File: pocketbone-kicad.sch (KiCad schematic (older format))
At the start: 73 parts, among them P1 USB_OTG, P2 USB_OTG, P3 CONN_01X10, SW1 SW_PUSH_SMALL_H, SW2 SW_PUSH_SMALL_H, U1 SN74LVC1G07, U2 OSD3358, U3 24LC32AT-I/OT, U4 TPS2051C, Y2 24MHz

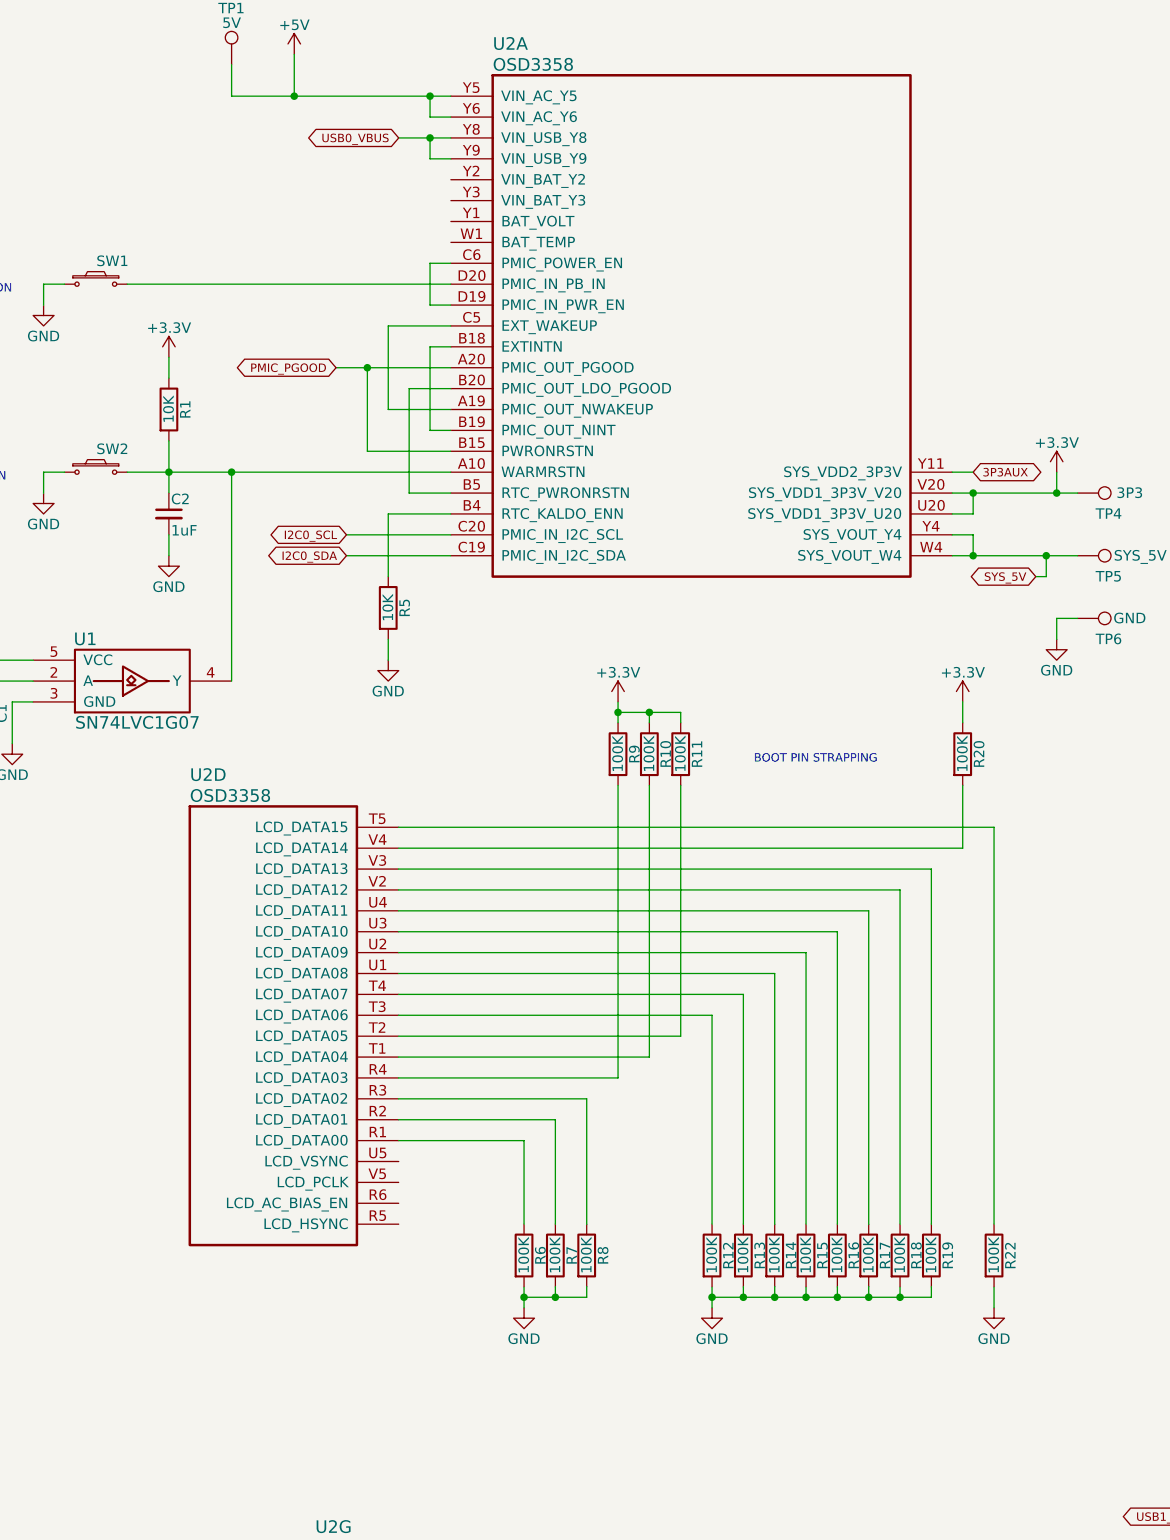
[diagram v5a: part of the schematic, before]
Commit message: Many PCB updates
Updated the placement for single sided population.
Switched boot mode selection resistors to arrays to save space.
Switched expansion header to .1 inch (lichen pub compatible).
Added battery connect similar to BBB.

Signed-off-by: Michael Welling <mwelling@ieee.org>
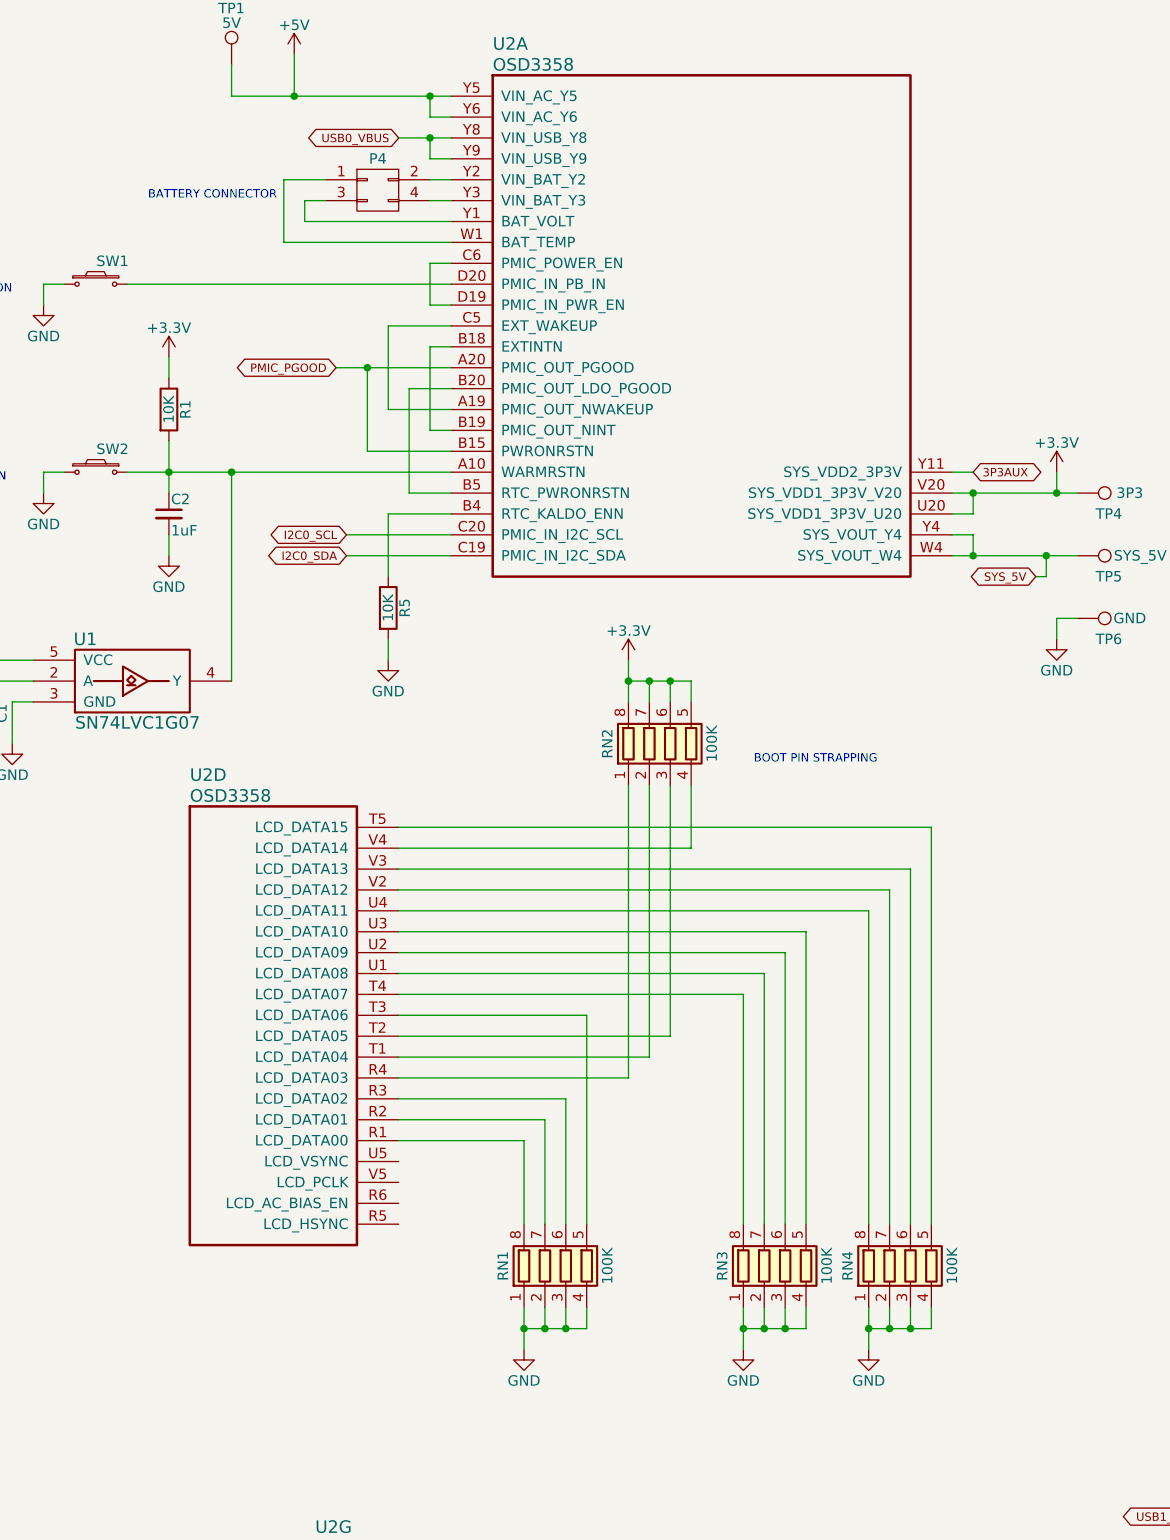
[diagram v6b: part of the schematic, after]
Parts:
- removed R10, R11, R12, R13, R14, R15, R16, R17, R18, R19, R20, R22, R6, R7, R8, R9: 100K, Resistors_SMD:R_0402, symbol R
- added P4: CONN_02X02, Socket_Strips:Socket_Strip_Straight_2x02, symbol CONN_02X02
- added RN1, RN2, RN3, RN4: 100K, Resistors_SMD:R_Array_Concave_4x0603, symbol R_Pack04
- P3: footprint Connectors_Molex:Connector_Molex_PicoBlade_53398-1071 -> Socket_Strips:Socket_Strip_Straight_1x10
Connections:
- net +3V3: now also RN2.5 (R4.2), RN2.6 (R3.2), RN2.7 (R2.2), RN2.8 (R1.2)
- net GND: now also RN1.1 (R1.1), RN1.2 (R2.1), RN1.3 (R3.1), RN1.4 (R4.1), RN3.1 (R1.1), RN3.2 (R2.1), RN3.3 (R3.1), RN3.4 (R4.1), RN4.1 (R1.1), RN4.2 (R2.1), RN4.3 (R3.1), RN4.4 (R4.1)
- net at U2.W1 (BAT_TEMP): now also P4.1 (P1)
- net at U2.Y1 (BAT_VOLT): now also P4.3 (P3)
- net at U2.Y2 (VIN_BAT_Y2): now also P4.2 (P2)
- net at U2.Y3 (VIN_BAT_Y3): now also P4.4 (P4)
- net at U2.R1 (LCD_DATA00): now also RN1.8 (R1.2)
- net at U2.R2 (LCD_DATA01): now also RN1.7 (R2.2)
- net at U2.R3 (LCD_DATA02): now also RN1.6 (R3.2)
- net at U2.R4 (LCD_DATA03): now also RN2.1 (R1.1)
- net at U2.T1 (LCD_DATA04): now also RN2.2 (R2.1)
- net at U2.T2 (LCD_DATA05): now also RN2.3 (R3.1)
- net at U2.T3 (LCD_DATA06): now also RN1.5 (R4.2)
- net at U2.T4 (LCD_DATA07): now also RN3.8 (R1.2)
- net at U2.T5 (LCD_DATA15): now also RN4.5 (R4.2)
- net at U2.U1 (LCD_DATA08): now also RN3.7 (R2.2)
- net at U2.U2 (LCD_DATA09): now also RN3.6 (R3.2)
- net at U2.U3 (LCD_DATA10): now also RN3.5 (R4.2)
- net at U2.U4 (LCD_DATA11): now also RN4.8 (R1.2)
- net at U2.V2 (LCD_DATA12): now also RN4.7 (R2.2)
- net at U2.V3 (LCD_DATA13): now also RN4.6 (R3.2)
- net at U2.V4 (LCD_DATA14): now also RN2.4 (R4.1)
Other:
- note added: "BATTERY CONNECTOR"

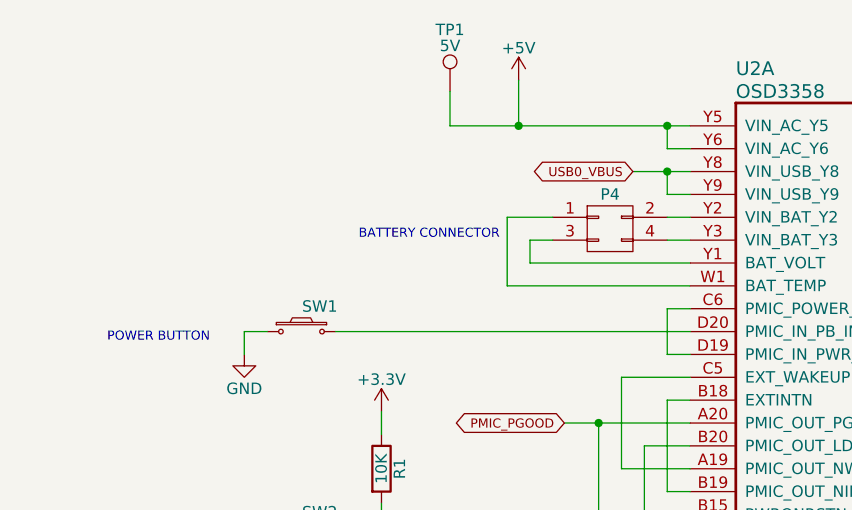
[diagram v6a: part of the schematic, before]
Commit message: Routing complete
Battery header updated in schmatic.
Plots and pictures updated.
Ready for design review.

Signed-off-by: Michael Welling <mwelling@ieee.org>
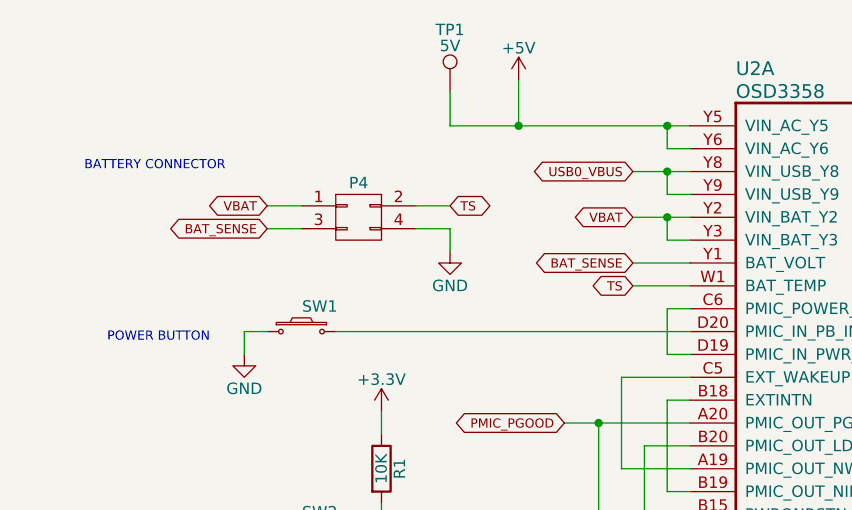
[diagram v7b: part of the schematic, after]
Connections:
- net GND: now also P4.4 (P4)
- net TS: now reaches U2.W1 (BAT_TEMP)
- net TS: now also P4.2 (P2); no longer P4.1 (P1)
- net BAT_SENSE: now reaches P4.3 (P3), U2.Y1 (BAT_VOLT)
- net VBAT: now reaches U2.Y2 (VIN_BAT_Y2)
- net VBAT: now also P4.1 (P1), U2.Y3 (VIN_BAT_Y3); no longer P4.2 (P2)
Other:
- moved on the sheet: P4

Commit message: Last minute tweaks
This version is posted to OSHpark site for anyone to order.
Order at your own risk.

Signed-off-by: Michael Welling <mwelling@ieee.org>
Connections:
- net GND: now also P1.6 (shield), P2.6 (shield)
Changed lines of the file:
@@
 Wire Wire Line
 	2400 2250 2400 2350
+$Comp
+L GND #PWR?
+U 1 1 589CA027
+P 9800 11250
+F 0 "#PWR?" H 9800 11000 50  0001 C CNN
+F 1 "GND" H 9800 11100 50  0000 C CNN
+F 2 "" H 9800 11250 50  0000 C CNN
+F 3 "" H 9800 11250 50  0000 C CNN
+	1    9800 11250
+	1    0    0    -1
+$EndComp
+$Comp
+L GND #PWR?
+U 1 1 589CA10D
+P 9800 9900
+F 0 "#PWR?" H 9800 9650 50  0001 C CNN
+F 1 "GND" H 9800 9750 50  0000 C CNN
+F 2 "" H 9800 9900 50  0000 C CNN
+F 3 "" H 9800 9900 50  0000 C CNN
+	1    9800 9900
+	1    0    0    -1
+$EndComp
 $EndSCHEMATC
